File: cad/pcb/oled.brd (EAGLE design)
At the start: 26.2 x 26.2 mm, 21 parts, among them U1 UG-2828GDEDF11, U2 FAN5331SX

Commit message: Revert "Revert OLED board to use 3.3V for input to the 13V FAN5331 boost"
This reverts commit 2f54354309870ccb091a2a633caf6ab9d6db30ca.
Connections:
- net +3V3: no longer C6.1, L1.P$1, U2.4, U2.5
- net VIN: now also C6.1, L1.P$1, U2.4, U2.5
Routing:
- net VIN: track 0.00 -> 25.2 mm
- net +3V3: track 53.8 -> 37.9 mm
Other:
- board text added: "BWS OLED V3"
- board text removed: "BWS OLED V4"
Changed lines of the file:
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@@
 <drawing>
 <settings>
-<setting alwaysvectorfont="no"/>
+<setting alwaysvectorfont="yes"/>
 <setting keepoldvectorfont="yes"/>
 <setting verticaltext="up"/>
@@
 <text x="2.794" y="4.572" size="0.8128" layer="26" rot="MR180" grouprefs="EVERYTHING">VIN</text>
 <text x="16.637" y="22.606" size="0.8128" layer="25" font="vector">BWS
-OLED V4</text>
+OLED V3</text>
 </plain>
 <attributes>
@@
 <via x="17.3736" y="8.4328" extent="1-16" drill="0.4"/>
 <via x="14.224" y="5.588" extent="1-16" drill="0.4"/>
-<contactref element="C6" pad="1"/>
-<contactref element="U2" pad="5"/>
-<contactref element="U2" pad="4"/>
-<contactref element="L1" pad="P$1"/>
-<wire x1="12.2936" y1="18.4912" x2="10.4648" y2="18.4912" width="0.4064" layer="1"/>
-<wire x1="10.4648" y1="18.4912" x2="10.43" y2="18.5119" width="0.4064" layer="1"/>
-<wire x1="12.2936" y1="18.4912" x2="12.33" y2="18.5119" width="0.4064" layer="1"/>
-<wire x1="10.4648" y1="16.9672" x2="10.4648" y2="15.4432" width="0.4064" layer="1"/>
-<wire x1="10.2616" y1="17.1704" x2="10.4648" y2="16.9672" width="0.4064" layer="1"/>
-<wire x1="10.2616" y1="17.78" x2="10.2616" y2="17.1704" width="0.4064" layer="1"/>
-<wire x1="10.4648" y1="17.9832" x2="10.2616" y2="17.78" width="0.4064" layer="1"/>
-<wire x1="10.4648" y1="18.288" x2="10.4648" y2="17.9832" width="0.4064" layer="1"/>
-<wire x1="10.4648" y1="15.4432" x2="10.483" y2="15.367" width="0.4064" layer="1"/>
-<wire x1="10.4648" y1="18.288" x2="10.43" y2="18.5119" width="0.4064" layer="1"/>
-<wire x1="13.208" y1="18.6944" x2="15.1384" y2="18.6944" width="0.4064" layer="1"/>
-<wire x1="13.1064" y1="18.5928" x2="13.208" y2="18.6944" width="0.4064" layer="1"/>
-<wire x1="12.4968" y1="18.5928" x2="13.1064" y2="18.5928" width="0.4064" layer="1"/>
-<wire x1="15.1384" y1="18.6944" x2="15.19" y2="18.685" width="0.4064" layer="1"/>
-<wire x1="12.4968" y1="18.5928" x2="12.33" y2="18.5119" width="0.4064" layer="1"/>
-<wire x1="6.7633375" y1="10.4346" x2="7.1284" y2="10.7996625" width="0.4064" layer="1"/>
-<wire x1="7.1284" y1="10.7996625" x2="7.1284" y2="12.1068" width="0.4064" layer="1"/>
-<wire x1="7.1284" y1="12.1068" x2="10.4648" y2="15.4432" width="0.4064" layer="1"/>
-<wire x1="5.845" y1="9.591" x2="6.6886" y2="10.4346" width="0.4064" layer="1"/>
-<wire x1="6.6886" y1="10.4346" x2="6.7633375" y2="10.4346" width="0.4064" layer="1"/>
 </signal>
 <signal name="D1/GPIO5">
@@
 </signal>
 <signal name="VIN" class="1">
+<contactref element="C6" pad="1"/>
+<contactref element="U2" pad="5"/>
+<contactref element="U2" pad="4"/>
+<contactref element="L1" pad="P$1"/>
 <contactref element="JP1" pad="8"/>
+<wire x1="12.2936" y1="18.4912" x2="10.4648" y2="18.4912" width="0.4064" layer="1"/>
+<wire x1="10.4648" y1="18.4912" x2="10.43" y2="18.5119" width="0.4064" layer="1"/>
+<wire x1="12.2936" y1="18.4912" x2="12.33" y2="18.5119" width="0.4064" layer="1"/>
+<wire x1="10.4648" y1="16.9672" x2="10.4648" y2="15.4432" width="0.4064" layer="1"/>
+<wire x1="10.2616" y1="17.1704" x2="10.4648" y2="16.9672" width="0.4064" layer="1"/>
+<wire x1="10.2616" y1="17.78" x2="10.2616" y2="17.1704" width="0.4064" layer="1"/>
+<wire x1="10.4648" y1="17.9832" x2="10.2616" y2="17.78" width="0.4064" layer="1"/>
+<wire x1="10.4648" y1="18.288" x2="10.4648" y2="17.9832" width="0.4064" layer="1"/>
+<wire x1="10.4648" y1="15.4432" x2="10.483" y2="15.367" width="0.4064" layer="1"/>
+<wire x1="10.4648" y1="18.288" x2="10.43" y2="18.5119" width="0.4064" layer="1"/>
+<wire x1="13.208" y1="18.6944" x2="15.1384" y2="18.6944" width="0.4064" layer="1"/>
+<wire x1="13.1064" y1="18.5928" x2="13.208" y2="18.6944" width="0.4064" layer="1"/>
+<wire x1="12.4968" y1="18.5928" x2="13.1064" y2="18.5928" width="0.4064" layer="1"/>
+<wire x1="15.1384" y1="18.6944" x2="15.19" y2="18.685" width="0.4064" layer="1"/>
+<wire x1="12.4968" y1="18.5928" x2="12.33" y2="18.5119" width="0.4064" layer="1"/>
+<wire x1="1.9304" y1="4.2672" x2="1.7272" y2="4.2672" width="0.4064" layer="1"/>
+<wire x1="3.9624" y1="6.2992" x2="1.9304" y2="4.2672" width="0.4064" layer="1"/>
+<wire x1="3.9624" y1="12.4968" x2="3.9624" y2="6.2992" width="0.4064" layer="1"/>
+<wire x1="6.604" y1="15.1384" x2="3.9624" y2="12.4968" width="0.4064" layer="1"/>
+<wire x1="10.2616" y1="15.1384" x2="6.604" y2="15.1384" width="0.4064" layer="1"/>
+<wire x1="10.3632" y1="15.24" x2="10.2616" y2="15.1384" width="0.4064" layer="1"/>
+<wire x1="1.7272" y1="4.2672" x2="1.651" y2="4.191" width="0.4064" layer="1"/>
+<wire x1="10.3632" y1="15.24" x2="10.483" y2="15.367" width="0.4064" layer="1"/>
 </signal>
 <signal name="D6/GPIO12/MISO">

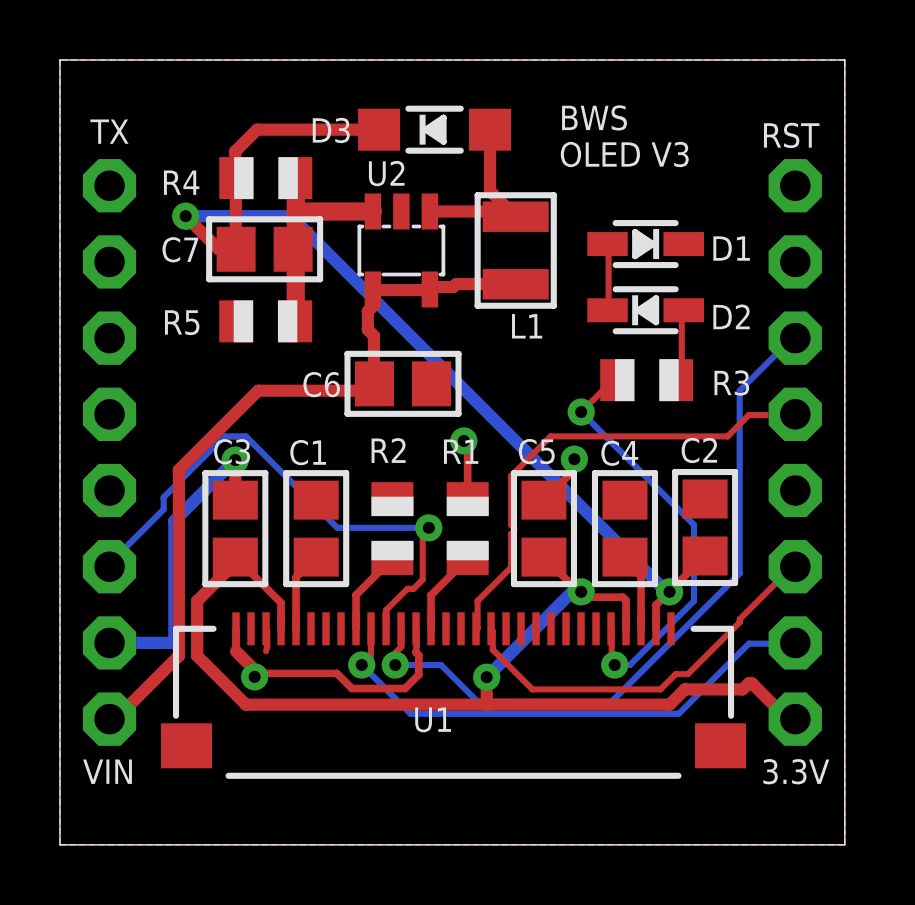
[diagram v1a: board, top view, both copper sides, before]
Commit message: Change reverted OLED to V5. Small GND trace cleanup.
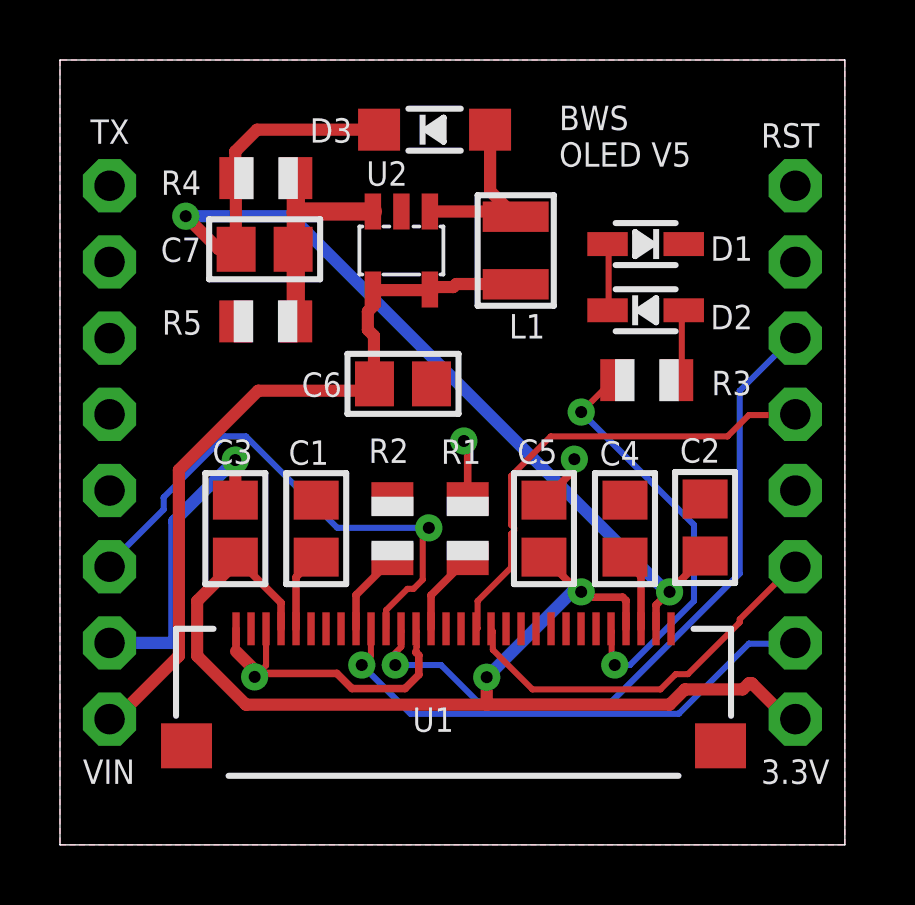
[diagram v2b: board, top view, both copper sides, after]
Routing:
- net GND: track 24.8 -> 25.8 mm
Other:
- board text added: "BWS OLED V5"
- board text removed: "BWS OLED V3"
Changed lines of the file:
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@@
 <?xml version="1.0" encoding="utf-8"?>
 <!DOCTYPE eagle SYSTEM "eagle.dtd">
-<eagle version="9.5.0">
+<eagle version="9.6.2">
 <drawing>
 <settings>
-<setting alwaysvectorfont="yes"/>
+<setting alwaysvectorfont="no"/>
 <setting keepoldvectorfont="yes"/>
 <setting verticaltext="up"/>
@@
 </layers>
 <board>
-<fusionsync huburn="a.cGVyc29uYWw6dWUyODFhMTI5" projecturn="a.cGVyc29uYWw6dWUyODFhMTI5IzIwMTkwOTE3MjE1ODk1MzI2" f3durn="urn:adsk.wipprod:dm.lineage:P5lhZWs8S_KHtQ88bDf2NQ" pcbguid="d3e705c3-1af4-4cef-b1e2-384e1dcb5e4e" lastpulledtime="" lastsyncedchangeguid="5ba198aa-53f5-64b5-e4eb-32003e20bcfd"/>
+<fusionsync huburn="a.cGVyc29uYWw6dWUyODFhMTI5" projecturn="a.cGVyc29uYWw6dWUyODFhMTI5IzIwMTkwOTE3MjE1ODk1MzI2" f3durn="urn:adsk.wipprod:dm.lineage:P5lhZWs8S_KHtQ88bDf2NQ" pcbguid="d3e705c3-1af4-4cef-b1e2-384e1dcb5e4e" lastpulledtime="" lastsyncedchangeguid="5ba198aa-53f5-64b5-e4eb-32003e20bcfd" latestrevisionid="" lastsyncedrevisionid="" lastboardhashguid="" lastpushedtime="" linktopcb3d="false"/>
 <plain>
 <wire x1="0" y1="26.162" x2="0" y2="0" width="0" layer="20" grouprefs="EVERYTHING"/>
@@
 <text x="2.794" y="4.572" size="0.8128" layer="26" rot="MR180" grouprefs="EVERYTHING">VIN</text>
 <text x="16.637" y="22.606" size="0.8128" layer="25" font="vector">BWS
-OLED V3</text>
+OLED V5</text>
 </plain>
 <attributes>
@@
 <contactref element="R1" pad="1"/>
 <contactref element="JP1" pad="7"/>
-<wire x1="6.9088" y1="6.604" x2="6.9088" y2="7.112" width="0.2032" layer="1"/>
-<wire x1="6.9088" y1="7.112" x2="6.868" y2="7.202" width="0.2032" layer="1"/>
-<wire x1="6.9088" y1="6.604" x2="6.86798125" y2="6.45225" width="0.2032" layer="1"/>
 <wire x1="11.8872" y1="6.604" x2="11.8872" y2="7.112" width="0.2032" layer="1"/>
 <wire x1="11.8872" y1="7.112" x2="11.868" y2="7.202" width="0.2032" layer="1"/>
@@
 <wire x1="13.589" y1="13.335" x2="13.462" y2="13.462" width="0.254" layer="1"/>
 <via x="13.462" y="13.462" extent="1-16" drill="0.4"/>
+<wire x1="6.488496875" y1="5.599496875" x2="6.868" y2="5.979" width="0.2032" layer="1"/>
+<wire x1="6.868" y1="5.979" x2="6.868" y2="7.202" width="0.2032" layer="1"/>
 </signal>
 <signal name="IREF">
